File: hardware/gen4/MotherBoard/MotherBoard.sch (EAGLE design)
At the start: 14 parts

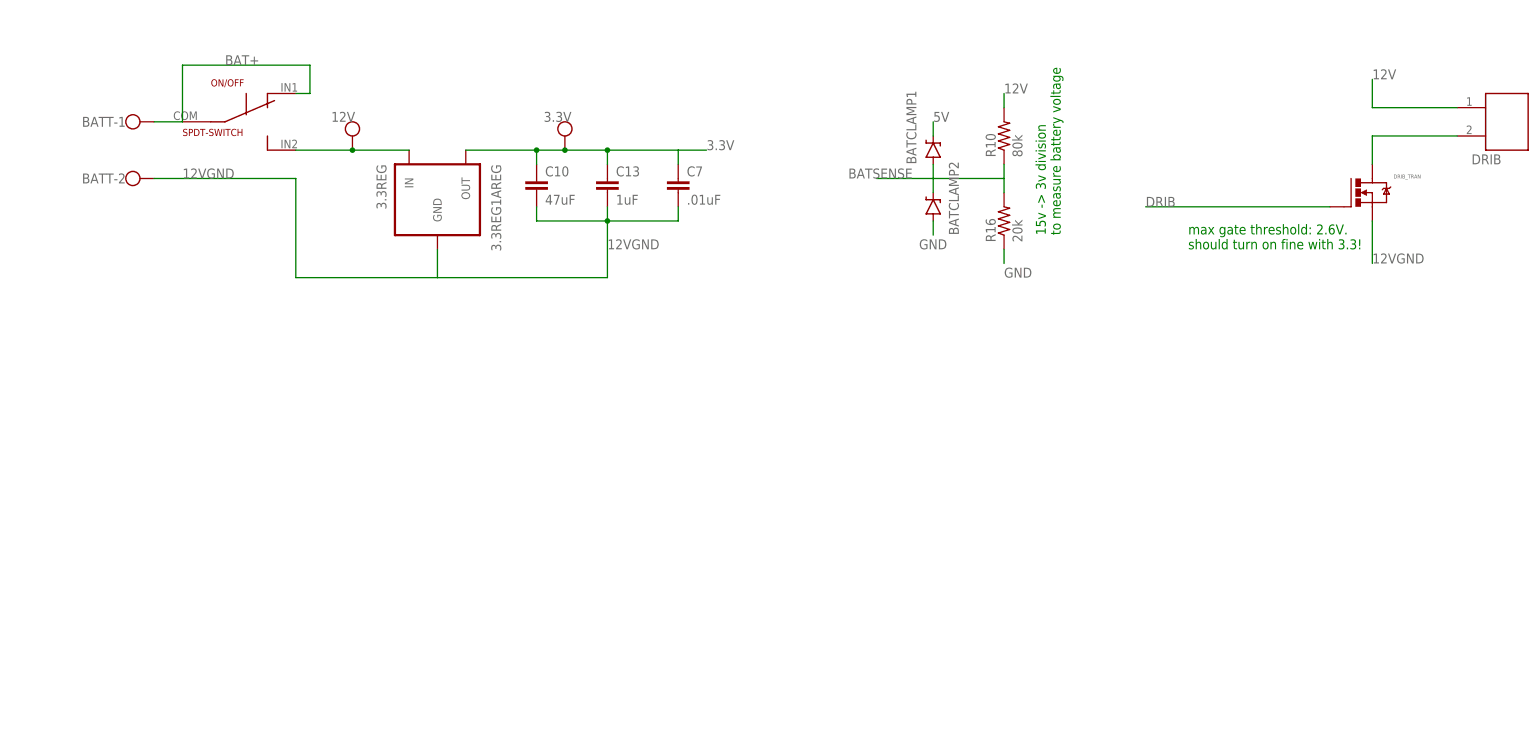
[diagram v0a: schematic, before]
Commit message: added neon light and caps. Changed Bat clamp to 3.3v and added junctions
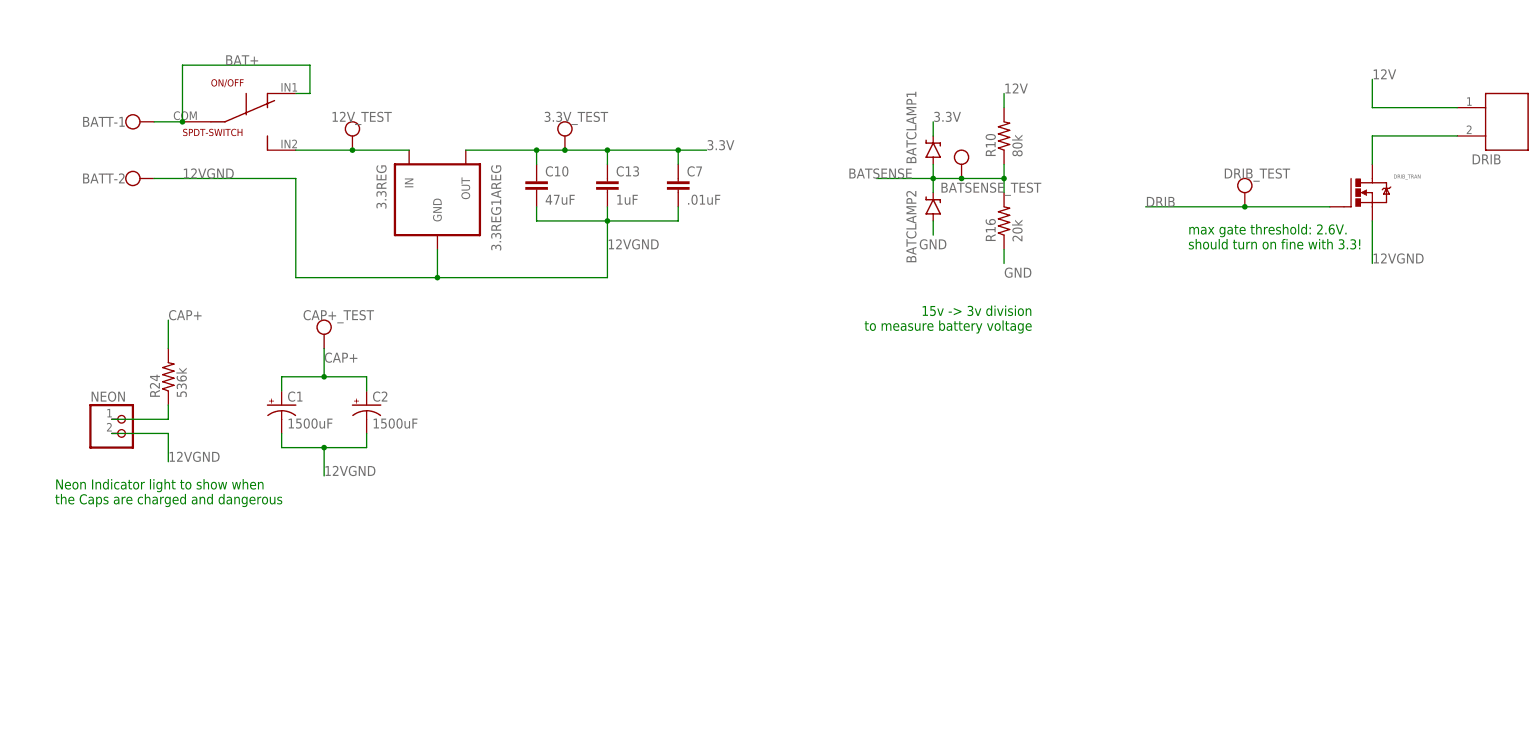
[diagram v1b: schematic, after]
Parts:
- added BATSENSE_TEST, CAP+_TEST, DRIB_TEST: TEST_PT, gen3:TEST_PT
- added C1, C2: 1500uF, rcl:CPOL-USE10-35
- added NEON: (no value), pinhead:PINHD-1X2
- added R24: 536k, SparkFun-Passives:RESISTOR0805-RES
- renumbered 12V to 12V_TEST, 3.3V to 3.3V_TEST
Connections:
- removed net 5V: BATCLAMP1.C
- new net CAP+: C1.+, C2.+, CAP+_TEST.P$1, R24.2
- new net TO_NEON: NEON.1, R24.1
- net 12VGND: now also C1.-, C2.-, NEON.2
- net 3.3V: now also BATCLAMP1.C
- net BATSENSE: now also BATSENSE_TEST.P$1
- net DRIB: now also DRIB_TEST.P$1
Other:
- note added: "Neon Indicator light to show when the Caps are charged and dangerous"
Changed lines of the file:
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@@
 <part name="C13" library="SparkFun-Capacitors" deviceset="CAP" device="0805" value="1uF"/>
 <part name="ON/OFF" library="gen3" deviceset="SPDT-SWITCH" device=""/>
-<part name="3.3V" library="gen3" deviceset="TEST_PT" device=""/>
+<part name="3.3V_TEST" library="gen3" deviceset="TEST_PT" device=""/>
 <part name="3.3REG" library="gen3" deviceset="3.3REG1A" device="REG"/>
 <part name="C7" library="SparkFun-Capacitors" deviceset="CAP" device="0805" value=".01uF"/>
@@
 <part name="R10" library="SparkFun-Passives" deviceset="RESISTOR" device="0805-RES" value="80k"/>
 <part name="R16" library="SparkFun-Passives" deviceset="RESISTOR" device="0805-RES" value="20k"/>
-<part name="12V" library="gen3" deviceset="TEST_PT" device=""/>
+<part name="12V_TEST" library="gen3" deviceset="TEST_PT" device=""/>
 <part name="BATCLAMP1" library="gen3" deviceset="DIODE-ZENER" device="DO214AC" value="DIODE-ZENERDO214AC"/>
 <part name="BATCLAMP2" library="gen3" deviceset="DIODE-ZENER" device="DO214AC" value="DIODE-ZENERDO214AC"/>
 <part name="DRIB_TRAN" library="gen3" deviceset="N-MOSFET" device="DPAK"/>
 <part name="DRIB" library="gen3" deviceset="JST-2" device="2MM"/>
+<part name="C1" library="rcl" deviceset="CPOL-US" device="E10-35" value="1500uF"/>
+<part name="C2" library="rcl" deviceset="CPOL-US" device="E10-35" value="1500uF"/>
+<part name="NEON" library="pinhead" deviceset="PINHD-1X2" device=""/>
+<part name="R24" library="SparkFun-Passives" deviceset="RESISTOR" device="0805-RES" value="536k"/>
+<part name="DRIB_TEST" library="gen3" deviceset="TEST_PT" device=""/>
+<part name="BATSENSE_TEST" library="gen3" deviceset="TEST_PT" device=""/>
+<part name="CAP+_TEST" library="gen3" deviceset="TEST_PT" device=""/>
 </parts>
 <sheets>
 <sheet>
 <plain>
-<text x="157.48" y="63.5" size="1.778" layer="91" rot="R90">15v -&gt; 3v division
+<text x="152.4" y="50.8" size="1.778" layer="91" rot="R180">15v -&gt; 3v division
 to measure battery voltage</text>
 <text x="180.34" y="60.96" size="1.778" layer="91">max gate threshold: 2.6V.
 should turn on fine with 3.3!</text>
+<text x="-22.86" y="15.24" size="1.778" layer="91">Neon Indicator light to show when
+the Caps are charged and dangerous</text>
 </plain>
 <instances>
@@
 <instance part="C13" gate="G$1" x="76.2" y="71.12"/>
 <instance part="ON/OFF" gate="G$1" x="10.16" y="83.82"/>
-<instance part="3.3V" gate="G$1" x="68.58" y="81.28"/>
+<instance part="3.3V_TEST" gate="G$1" x="68.58" y="81.28"/>
 <instance part="3.3REG" gate="G$1" x="45.72" y="71.12" rot="MR270"/>
 <instance part="C7" gate="G$1" x="88.9" y="71.12"/>
@@
 <instance part="R10" gate="G$1" x="147.32" y="81.28" rot="R90"/>
 <instance part="R16" gate="G$1" x="147.32" y="66.04" rot="R90"/>
-<instance part="12V" gate="G$1" x="30.48" y="81.28"/>
+<instance part="12V_TEST" gate="G$1" x="30.48" y="81.28"/>
 <instance part="BATCLAMP1" gate="G$1" x="134.62" y="78.74" smashed="yes" rot="R90">
 <attribute name="NAME" x="131.5974" y="76.2" size="1.778" layer="95" rot="R90"/>
 </instance>
 <instance part="BATCLAMP2" gate="G$1" x="134.62" y="68.58" smashed="yes" rot="R90">
-<attribute name="NAME" x="139.2174" y="63.5" size="1.778" layer="95" rot="R90"/>
+<attribute name="NAME" x="131.5974" y="58.42" size="1.778" layer="95" rot="R90"/>
 </instance>
 <instance part="DRIB_TRAN" gate="G$1" x="210.82" y="71.12"/>
 <instance part="DRIB" gate="G$1" x="233.68" y="83.82"/>
+<instance part="C1" gate="G$1" x="17.78" y="33.02"/>
+<instance part="C2" gate="G$1" x="33.02" y="33.02"/>
+<instance part="NEON" gate="G$1" x="-10.16" y="27.94"/>
+<instance part="R24" gate="G$1" x="-2.54" y="38.1" rot="R90"/>
+<instance part="DRIB_TEST" gate="G$1" x="190.5" y="71.12"/>
+<instance part="BATSENSE_TEST" gate="G$1" x="139.7" y="76.2" smashed="yes">
+<attribute name="NAME" x="135.89" y="71.12" size="1.778" layer="95"/>
+</instance>
+<instance part="CAP+_TEST" gate="G$1" x="25.4" y="45.72"/>
 </instances>
 <busses>
@@
 <pinref part="C7" gate="G$1" pin="1"/>
 <wire x1="88.9" y1="78.74" x2="88.9" y2="76.2" width="0.1524" layer="91"/>
-<pinref part="3.3V" gate="G$1" pin="P$1"/>
+<pinref part="3.3V_TEST" gate="G$1" pin="P$1"/>
 <wire x1="76.2" y1="78.74" x2="68.58" y2="78.74" width="0.1524" layer="91"/>
 <junction x="76.2" y="78.74"/>
@@
 <pinref part="C10" gate="G$1" pin="1"/>
 <wire x1="88.9" y1="78.74" x2="93.98" y2="78.74" width="0.1524" layer="91"/>
+<junction x="88.9" y="78.74"/>
+</segment>
+<segment>
+<pinref part="BATCLAMP1" gate="G$1" pin="C"/>
+<wire x1="134.62" y1="81.28" x2="134.62" y2="83.82" width="0.1524" layer="91"/>
+<label x="134.62" y="83.82" size="1.778" layer="95"/>
 </segment>
 </net>
@@
 <pinref part="3.3REG" gate="G$1" pin="GND"/>
 <wire x1="45.72" y1="60.96" x2="45.72" y2="55.88" width="0.1524" layer="91"/>
+<junction x="45.72" y="55.88"/>
 </segment>
 <segment>
@@
 <label x="213.36" y="58.42" size="1.778" layer="95"/>
 <pinref part="DRIB_TRAN" gate="G$1" pin="S"/>
+</segment>
+<segment>
+<pinref part="C1" gate="G$1" pin="-"/>
+<wire x1="17.78" y1="27.94" x2="17.78" y2="25.4" width="0.1524" layer="91"/>
+<pinref part="C2" gate="G$1" pin="-"/>
+<wire x1="17.78" y1="25.4" x2="25.4" y2="25.4" width="0.1524" layer="91"/>
+<wire x1="25.4" y1="25.4" x2="33.02" y2="25.4" width="0.1524" layer="91"/>
+<wire x1="33.02" y1="25.4" x2="33.02" y2="27.94" width="0.1524" layer="91"/>
+<junction x="25.4" y="25.4"/>
+<wire x1="25.4" y1="25.4" x2="25.4" y2="20.32" width="0.1524" layer="91"/>
+<label x="25.4" y="20.32" size="1.778" layer="95"/>
+</segment>
+<segment>
+<pinref part="NEON" gate="G$1" pin="2"/>
+<wire x1="-12.7" y1="27.94" x2="-2.54" y2="27.94" width="0.1524" layer="91"/>
+<wire x1="-2.54" y1="27.94" x2="-2.54" y2="22.86" width="0.1524" layer="91"/>
+<label x="-2.54" y="22.86" size="1.778" layer="95"/>
 </segment>
 </net>
@@
 <wire x1="22.86" y1="88.9" x2="20.32" y2="88.9" width="0.1524" layer="91"/>
 <label x="7.62" y="93.98" size="1.778" layer="95"/>
+<junction x="0" y="83.82"/>
 </segment>
 </net>
@@
 <pinref part="ON/OFF" gate="G$1" pin="P2"/>
 <wire x1="20.32" y1="78.74" x2="30.48" y2="78.74" width="0.1524" layer="91"/>
-<pinref part="12V" gate="G$1" pin="P$1"/>
+<pinref part="12V_TEST" gate="G$1" pin="P$1"/>
 <wire x1="30.48" y1="78.74" x2="40.64" y2="78.74" width="0.1524" layer="91"/>
 <junction x="30.48" y="78.74"/>
@@
 <wire x1="147.32" y1="71.12" x2="147.32" y2="73.66" width="0.1524" layer="91"/>
 <wire x1="147.32" y1="73.66" x2="147.32" y2="76.2" width="0.1524" layer="91"/>
-<wire x1="147.32" y1="73.66" x2="134.62" y2="73.66" width="0.1524" layer="91"/>
+<wire x1="147.32" y1="73.66" x2="139.7" y2="73.66" width="0.1524" layer="91"/>
 <label x="119.38" y="73.66" size="1.778" layer="95"/>
 <pinref part="BATCLAMP2" gate="G$1" pin="C"/>
+<wire x1="139.7" y1="73.66" x2="134.62" y2="73.66" width="0.1524" layer="91"/>
 <wire x1="134.62" y1="73.66" x2="124.46" y2="73.66" width="0.1524" layer="91"/>
 <wire x1="134.62" y1="71.12" x2="134.62" y2="73.66" width="0.1524" layer="91"/>
 <pinref part="BATCLAMP1" gate="G$1" pin="A"/>
 <wire x1="134.62" y1="76.2" x2="134.62" y2="73.66" width="0.1524" layer="91"/>
-</segment>
-</net>
-<net name="5V" class="0">
-<segment>
-<pinref part="BATCLAMP1" gate="G$1" pin="C"/>
-<wire x1="134.62" y1="81.28" x2="134.62" y2="83.82" width="0.1524" layer="91"/>
-<label x="134.62" y="83.82" size="1.778" layer="95"/>
+<pinref part="BATSENSE_TEST" gate="G$1" pin="P$1"/>
+<junction x="139.7" y="73.66"/>
+<junction x="147.32" y="73.66"/>
+<junction x="134.62" y="73.66"/>
 </segment>
 </net>
 <net name="DRIB" class="0">
 <segment>
-<wire x1="205.74" y1="68.58" x2="172.72" y2="68.58" width="0.1524" layer="91"/>
+<wire x1="205.74" y1="68.58" x2="190.5" y2="68.58" width="0.1524" layer="91"/>
 <label x="172.72" y="68.58" size="1.778" layer="95"/>
 <pinref part="DRIB_TRAN" gate="G$1" pin="G"/>
+<pinref part="DRIB_TEST" gate="G$1" pin="P$1"/>
+<wire x1="190.5" y1="68.58" x2="172.72" y2="68.58" width="0.1524" layer="91"/>
+<junction x="190.5" y="68.58"/>
 </segment>
 </net>
@@
 </segment>
 </net>
+<net name="CAP+" class="0">
+<segment>
+<pinref part="C1" gate="G$1" pin="+"/>
+<wire x1="17.78" y1="35.56" x2="17.78" y2="38.1" width="0.1524" layer="91"/>
+<wire x1="17.78" y1="38.1" x2="25.4" y2="38.1" width="0.1524" layer="91"/>
+<pinref part="C2" gate="G$1" pin="+"/>
+<wire x1="25.4" y1="38.1" x2="33.02" y2="38.1" width="0.1524" layer="91"/>
+<wire x1="33.02" y1="38.1" x2="33.02" y2="35.56" width="0.1524" layer="91"/>
+<wire x1="25.4" y1="38.1" x2="25.4" y2="43.18" width="0.1524" layer="91"/>
+<junction x="25.4" y="38.1"/>
+<label x="25.4" y="40.64" size="1.778" layer="95"/>
+<pinref part="CAP+_TEST" gate="G$1" pin="P$1"/>
+</segment>
+<segment>
+<pinref part="R24" gate="G$1" pin="2"/>
+<wire x1="-2.54" y1="43.18" x2="-2.54" y2="48.26" width="0.1524" layer="91"/>
+<label x="-2.54" y="48.26" size="1.778" layer="95"/>
+</segment>
+</net>
+<net name="TO_NEON" class="0">
+<segment>
+<pinref part="R24" gate="G$1" pin="1"/>
+<wire x1="-2.54" y1="33.02" x2="-2.54" y2="30.48" width="0.1524" layer="91"/>
+<pinref part="NEON" gate="G$1" pin="1"/>
+<wire x1="-2.54" y1="30.48" x2="-12.7" y2="30.48" width="0.1524" layer="91"/>
+</segment>
+</net>
 </nets>
 </sheet>
 </sheets>
+<errors>
+</errors>
 </schematic>
 </drawing>

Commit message: added motor boards
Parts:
- added FUSE_MOTOR3, FUSE_MOTOR_1, FUSE_MOTOR_2, FUSE_MOTOR_4: (no value), fuse:TR5
- added MOTORBOARD_HEADER1, MOTORBOARD_HEADER2, MOTORBOARD_HEADER3, MOTORBOARD_HEADER4: M10SILK_FEMALE_PTH, SparkFun-Connectors:M10SILK_FEMALE_PTH
- added POLARITY_PROTECT: BAT60J, diode:BAT60J
- added TMP: 0, SparkFun-Passives:RESISTOR0805-RES
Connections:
- new net 12V_MOTOR_1: FUSE_MOTOR_1.2
- new net 12V_MOTOR_2: FUSE_MOTOR_2.2
- new net 12V_MOTOR_3: FUSE_MOTOR3.2
- new net 12V_MOTOR_4: FUSE_MOTOR_4.2
- new net 5V: BATCLAMP1.C
- new net BAT+_UNPROTECTED: BATT-1.KL, POLARITY_PROTECT.A
- new net MISO: MOTORBOARD_HEADER1.2, MOTORBOARD_HEADER2.2, MOTORBOARD_HEADER3.2, MOTORBOARD_HEADER4.2
- new net MOSI: MOTORBOARD_HEADER1.3, MOTORBOARD_HEADER2.3, MOTORBOARD_HEADER3.3, MOTORBOARD_HEADER4.3
- new net SCLK: MOTORBOARD_HEADER1.4, MOTORBOARD_HEADER2.4, MOTORBOARD_HEADER3.4, MOTORBOARD_HEADER4.4
- new net SS1: MOTORBOARD_HEADER1.5
- new net SS2: MOTORBOARD_HEADER2.5
- new net SS3: MOTORBOARD_HEADER3.5
- new net SS4: MOTORBOARD_HEADER4.5
- net 12V: now also FUSE_MOTOR3.1, FUSE_MOTOR_1.1, FUSE_MOTOR_2.1, FUSE_MOTOR_4.1
- net 12VGND: now also MOTORBOARD_HEADER1.7, MOTORBOARD_HEADER2.7, MOTORBOARD_HEADER3.7, MOTORBOARD_HEADER4.7, TMP.1
- net 3.3V: no longer BATCLAMP1.C
- net BAT+: now also POLARITY_PROTECT.C; no longer BATT-1.KL
- net GND: now also MOTORBOARD_HEADER1.6, MOTORBOARD_HEADER2.6, MOTORBOARD_HEADER3.6, MOTORBOARD_HEADER4.6, TMP.2
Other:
- moved on the sheet: BATT-1, BATT-2

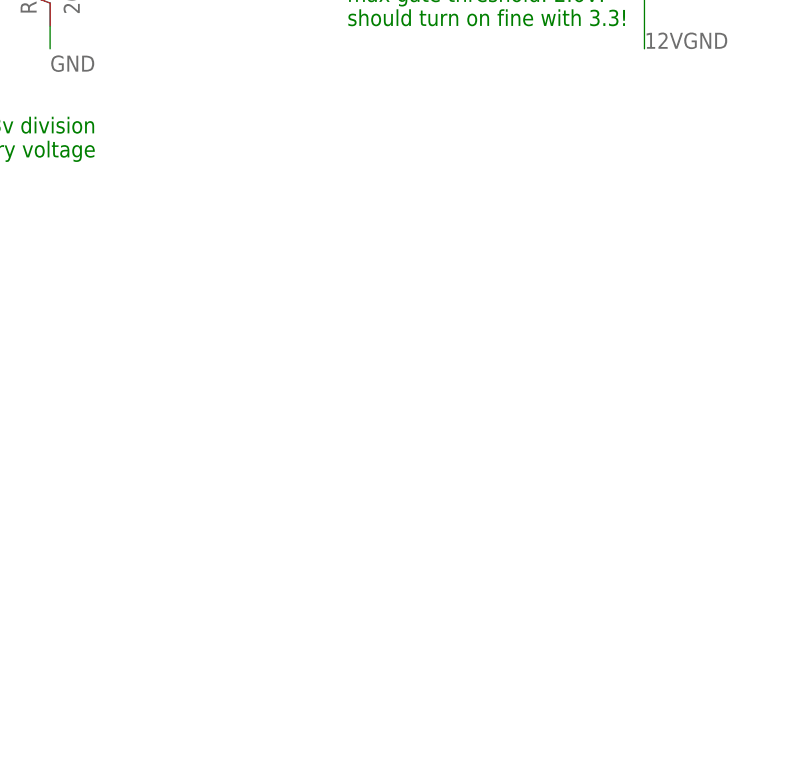
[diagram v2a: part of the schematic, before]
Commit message: Breakbeam
Added breakbeam to Motherboard. Let me know if this looks okay
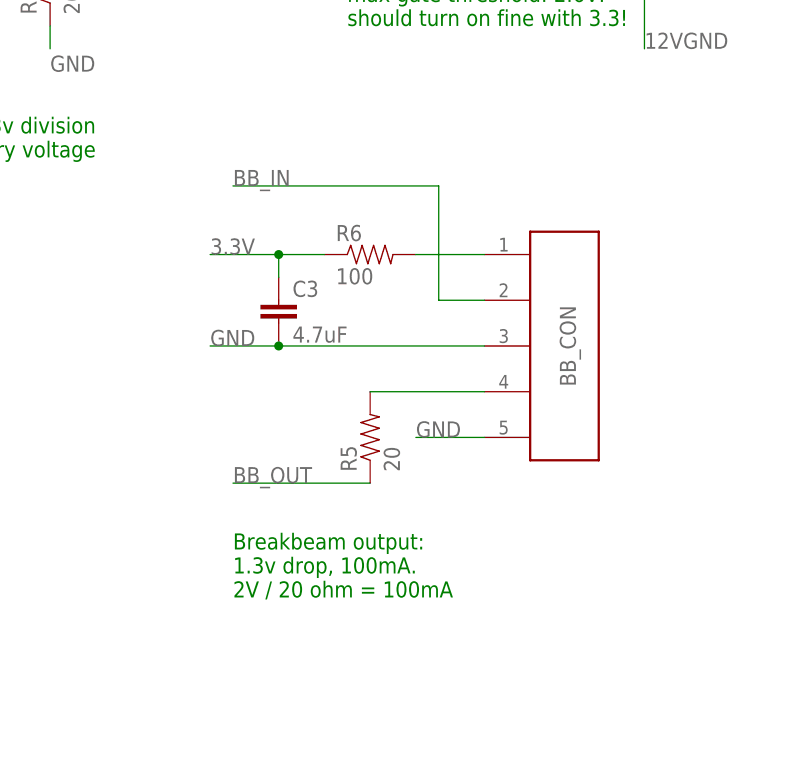
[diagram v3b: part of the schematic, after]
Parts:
- added BB_CON: JST-5, gen3:JST-5
- added C3: 4.7uF, SparkFun-Capacitors:CAP0805
- added R5: 20, SparkFun-Passives:RESISTOR0805-RES
- added R6: 100, SparkFun-Passives:RESISTOR0805-RES
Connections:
- new net BB_IN: BB_CON.P$2
- new net BB_OUT: R5.1
- new net N$32: BB_CON.P$4, R5.2
- new net N$40: BB_CON.P$1, R6.2
- net 3.3V: now also C3.1, R6.1
- net GND: now also BB_CON.P$3, BB_CON.P$5, C3.2
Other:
- note added: "Breakbeam output: 1.3v drop, 100mA. 2V / 20 ohm = 100mA"
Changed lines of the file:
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@@
 <part name="FUSE_MOTOR3" library="fuse" deviceset="TR5" device=""/>
 <part name="FUSE_MOTOR_4" library="fuse" deviceset="TR5" device=""/>
+<part name="R5" library="SparkFun-Passives" deviceset="RESISTOR" device="0805-RES" value="20"/>
+<part name="C3" library="SparkFun-Capacitors" deviceset="CAP" device="0805" value="4.7uF"/>
+<part name="R6" library="SparkFun-Passives" deviceset="RESISTOR" device="0805-RES" value="100"/>
+<part name="BB_CON" library="gen3" deviceset="JST-5" device=""/>
 </parts>
 <sheets>
@@
 <text x="-22.86" y="15.24" size="1.778" layer="91">Neon Indicator light to show when
 the Caps are charged and dangerous</text>
+<text x="167.64" y="-2.54" size="1.778" layer="91">Breakbeam output:
+1.3v drop, 100mA.
+2V / 20 ohm = 100mA</text>
 </plain>
 <instances>
@@
 <attribute name="VALUE" x="92.71" y="-0.381" size="1.778" layer="96"/>
 </instance>
+<instance part="R5" gate="G$1" x="182.88" y="15.24" rot="R90"/>
+<instance part="C3" gate="G$1" x="172.72" y="27.94"/>
+<instance part="R6" gate="G$1" x="182.88" y="35.56"/>
+<instance part="BB_CON" gate="G$1" x="203.2" y="25.4"/>
 </instances>
 <busses>
@@
 <wire x1="88.9" y1="78.74" x2="93.98" y2="78.74" width="0.1524" layer="91"/>
 <junction x="88.9" y="78.74"/>
+</segment>
+<segment>
+<pinref part="R6" gate="G$1" pin="1"/>
+<pinref part="C3" gate="G$1" pin="1"/>
+<wire x1="177.8" y1="35.56" x2="172.72" y2="35.56" width="0.1524" layer="91"/>
+<wire x1="172.72" y1="35.56" x2="172.72" y2="33.02" width="0.1524" layer="91"/>
+<wire x1="172.72" y1="35.56" x2="165.1" y2="35.56" width="0.1524" layer="91"/>
+<junction x="172.72" y="35.56"/>
+<label x="165.1" y="35.56" size="1.778" layer="95"/>
 </segment>
 </net>
@@
 <junction x="104.14" y="-10.16"/>
 </segment>
+<segment>
+<wire x1="195.58" y1="15.24" x2="187.96" y2="15.24" width="0.1524" layer="91"/>
+<label x="187.96" y="15.24" size="1.778" layer="95"/>
+<pinref part="BB_CON" gate="G$1" pin="P$5"/>
+</segment>
+<segment>
+<wire x1="195.58" y1="25.4" x2="172.72" y2="25.4" width="0.1524" layer="91"/>
+<pinref part="C3" gate="G$1" pin="2"/>
+<wire x1="172.72" y1="25.4" x2="165.1" y2="25.4" width="0.1524" layer="91"/>
+<junction x="172.72" y="25.4"/>
+<label x="165.1" y="25.4" size="1.778" layer="95"/>
+<pinref part="BB_CON" gate="G$1" pin="P$3"/>
+</segment>
 </net>
 <net name="12V" class="0">
@@
 </segment>
 </net>
+<net name="BB_OUT" class="0">
+<segment>
+<wire x1="167.64" y1="10.16" x2="182.88" y2="10.16" width="0.1524" layer="91"/>
+<pinref part="R5" gate="G$1" pin="1"/>
+<label x="167.64" y="10.16" size="1.778" layer="95"/>
+</segment>
+</net>
+<net name="BB_IN" class="0">
+<segment>
+<wire x1="195.58" y1="30.48" x2="190.5" y2="30.48" width="0.1524" layer="91"/>
+<wire x1="190.5" y1="30.48" x2="190.5" y2="43.18" width="0.1524" layer="91"/>
+<wire x1="190.5" y1="43.18" x2="167.64" y2="43.18" width="0.1524" layer="91"/>
+<label x="167.64" y="43.18" size="1.778" layer="95"/>
+<pinref part="BB_CON" gate="G$1" pin="P$2"/>
+</segment>
+</net>
+<net name="N$32" class="0">
+<segment>
+<pinref part="R5" gate="G$1" pin="2"/>
+<wire x1="195.58" y1="20.32" x2="182.88" y2="20.32" width="0.1524" layer="91"/>
+<pinref part="BB_CON" gate="G$1" pin="P$4"/>
+</segment>
+</net>
+<net name="N$40" class="0">
+<segment>
+<pinref part="R6" gate="G$1" pin="2"/>
+<wire x1="187.96" y1="35.56" x2="195.58" y2="35.56" width="0.1524" layer="91"/>
+<pinref part="BB_CON" gate="G$1" pin="P$1"/>
+</segment>
+</net>
